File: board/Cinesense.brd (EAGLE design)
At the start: 37 x 14.8 mm, 7 parts, among them J1 AVR_SPI_PROG_3X2PTH, P1 DE9-PCB-EDGEMALE, P2 DE9-PCB-EDGEFEMALE, U1 ATTINY85-20PU

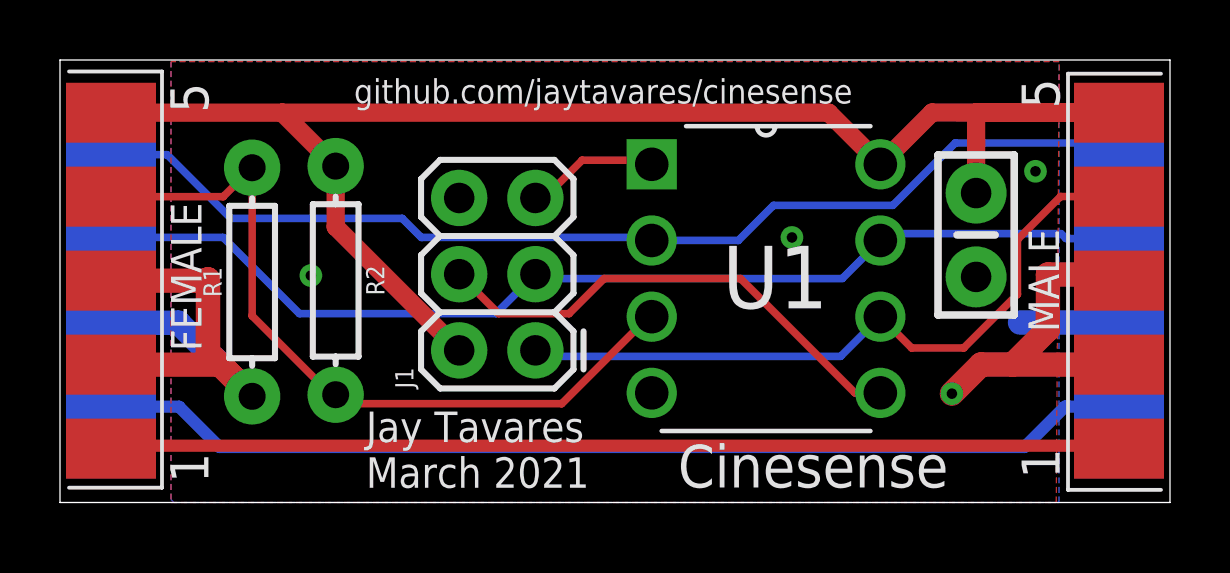
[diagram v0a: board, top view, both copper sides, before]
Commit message: Connect analog audio signals to inputs
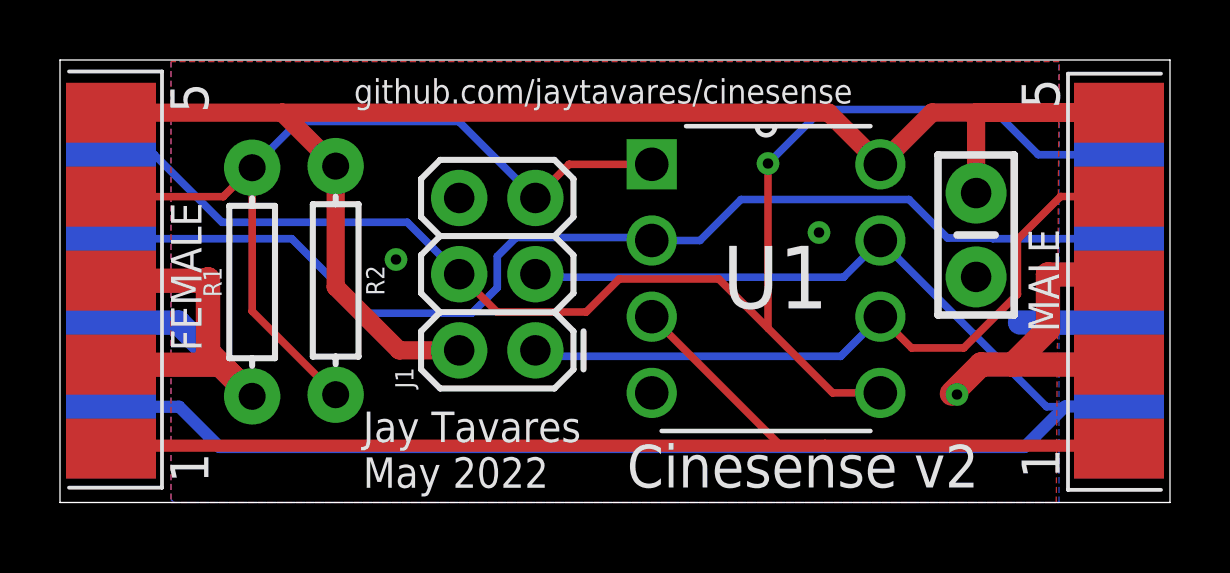
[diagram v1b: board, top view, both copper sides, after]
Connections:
- removed net MOSI: J1.4, U1.5
- removed net RST: J1.5, U1.1
- net ANALOG_LEFT+: now also J1.3, U1.7
- net ANALOG_RIGHT+: now also U1.3
- net CTRL_IN: now also J1.5, U1.1; no longer U1.3
- net IR: now also J1.4, U1.5; no longer U1.2
- net OPTICAL_AUDIO: now also U1.2; no longer J1.3, U1.7
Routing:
- net ANALOG_LEFT+: track 34.7 -> 57.0 mm
- net MOSI: track 16.6 -> 0.00 mm
- net IR: track 36.3 -> 48.4 mm, vias 0 -> 1
- net ANALOG_RIGHT+: track 33.7 -> 41.2 mm
- net RST: track 4.46 -> 0.00 mm
- net CTRL_IN: track 25.8 -> 29.3 mm
- net OPTICAL_AUDIO: track 36.0 -> 37.4 mm
- net VCC: track 52.8 -> 54.0 mm
- net GND: vias 4 -> 3
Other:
- board text added: "Cinesense v2"
- board text added: "Jay Tavares May 2022"
- board text removed: "Cinesense"
- board text removed: "Jay Tavares March 2021"
